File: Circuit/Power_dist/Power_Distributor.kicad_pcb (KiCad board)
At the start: 2 copper layers, 150.2 x 108.9 mm, 97 parts, among them CON1 Conn-PCIE-x16, J1 Thruster_Off_Switch, P1 XT60, P11 XT60, P15 USB_B, P16 XT60, P17 XT60, P2 XT30, P3 XT30, P4 XT30, P5 XT30, Q1 IPD90P03P4L, Q2 IPD90P03P4L, Q3 IPD90P03P4L, Q5 IPD90P03P4L, Q6 AUIRFS8409-7P, Q7 AUIRFS8409-7P, U1 93LC56BT-I/OT, U2 FT232H, U3 ACPL-247-500E, U4 ACPL-247-500E, U5 LTC4357, U6 LTC4357, U7 UWE-12/6-Q12P, U8 TEN_20-2411WIN, Y1 12MHz

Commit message: route pcb except gnd
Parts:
- moved C13 42.4 mm to (100.3, 116.6)
- moved C14 42.4 mm to (94.2, 113.5)
- moved C15 42.4 mm to (100.0, 113.5)
- moved C17 42.4 mm to (106.1, 113.5)
- moved C3 42.4 mm to (58.4, 107.4)
- moved C5 42.4 mm to (89.0, 121.2)
- moved C6 42.4 mm to (81.5, 112.0)
- moved C7 42.4 mm to (94.2, 110.5)
- moved C8 42.4 mm to (83.6, 121.2)
- moved D7 42.4 mm to (74.9, 117.3)
- moved L2 42.4 mm to (100.1, 110.5)
- moved P15 42.4 mm to (58.7, 126.7)
- moved R10 42.4 mm to (70.2, 117.3)
- moved R17 42.4 mm to (73.6, 106.4)
- moved R18 42.4 mm to (64.7, 117.3)
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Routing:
- net +BATT: track 0.00 -> 356.9 mm
- net +5V: track 0.00 -> 218.3 mm, vias 0 -> 2
- net /Kill_SW: track 5.00 -> 174.6 mm, vias 0 -> 1
- net +12V: track 0.00 -> 165.6 mm
- net /Power_Controller/SW1_C: track 14.3 -> 175.4 mm, vias 0 -> 2
- net /Power_Controller/SW4_C: track 15.8 -> 138.2 mm, vias 0 -> 2
- net /Power_Controller/SW3_C: track 30.8 -> 152.7 mm, vias 0 -> 2
- net Net-(C12-Pad1): track 9.53 -> 119.1 mm, vias 0 -> 2
- net +3V3: track 108.7 -> 175.0 mm, vias 0 -> 2
- net /Power_Controller/SW2_C: track 18.1 -> 73.5 mm, vias 0 -> 2
- net Net-(JP1-Pad2): track 0.00 -> 53.3 mm
- net Net-(D8-Pad2): track 0.00 -> 36.9 mm
- net Net-(D13-Pad2): track 0.00 -> 33.9 mm
- net Net-(F2-Pad2): track 0.00 -> 31.5 mm
- net Net-(C13-Pad1): track 37.3 -> 63.2 mm
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
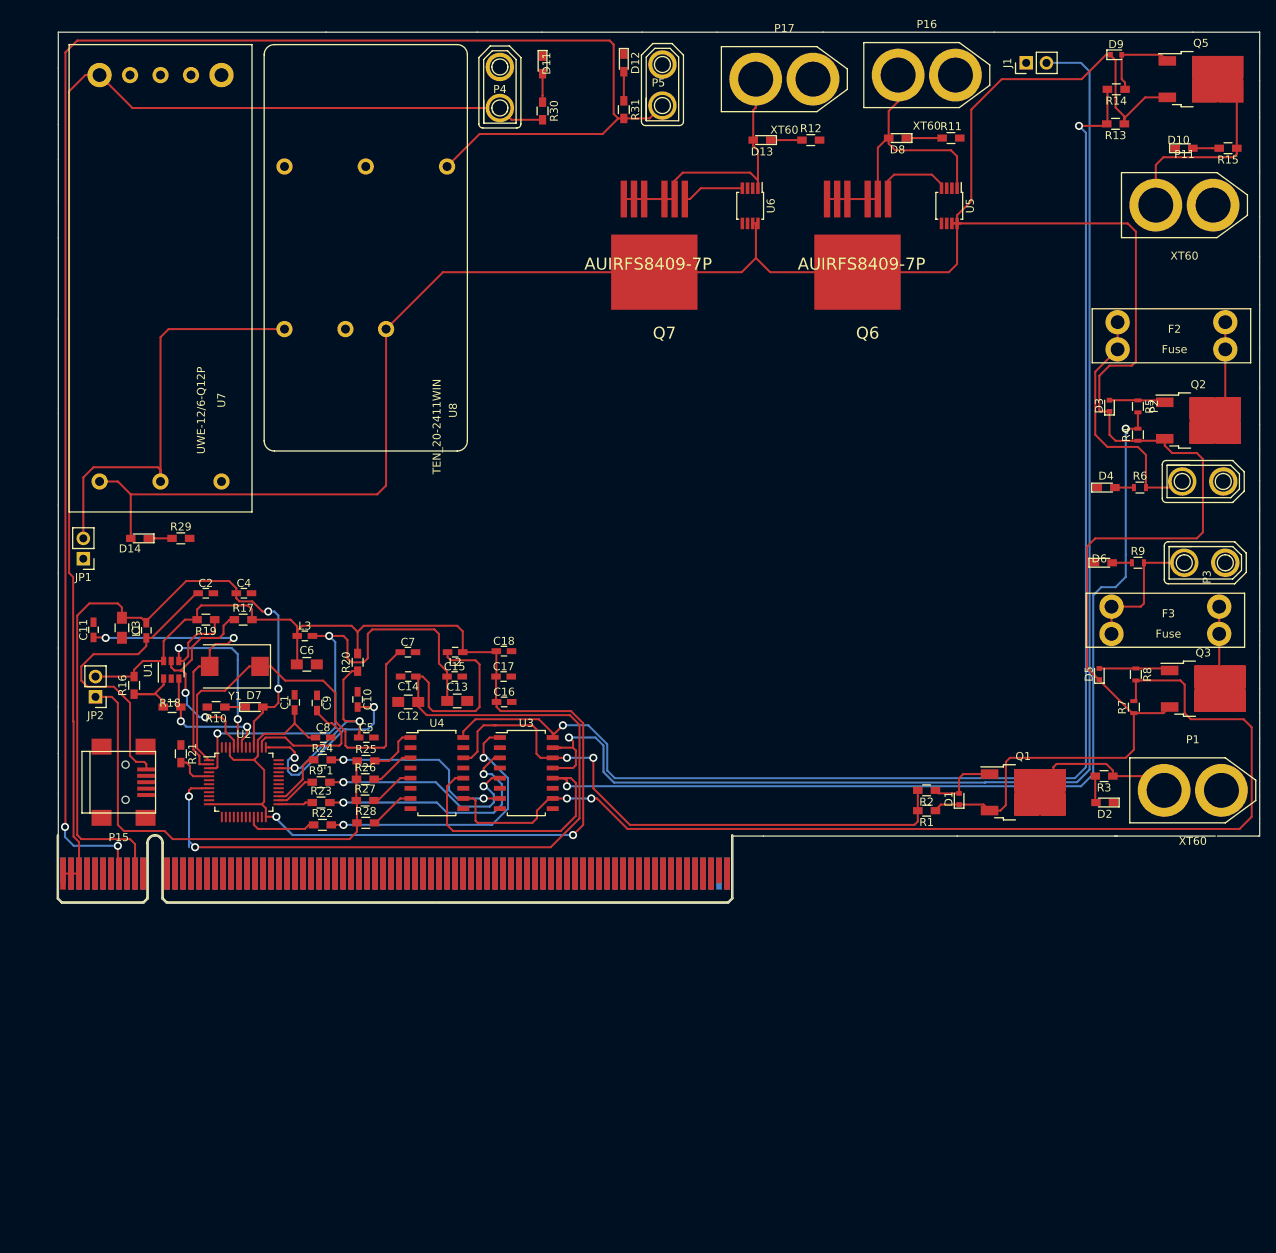
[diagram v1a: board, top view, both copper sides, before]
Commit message: add Vbatt plane, re-arrange components
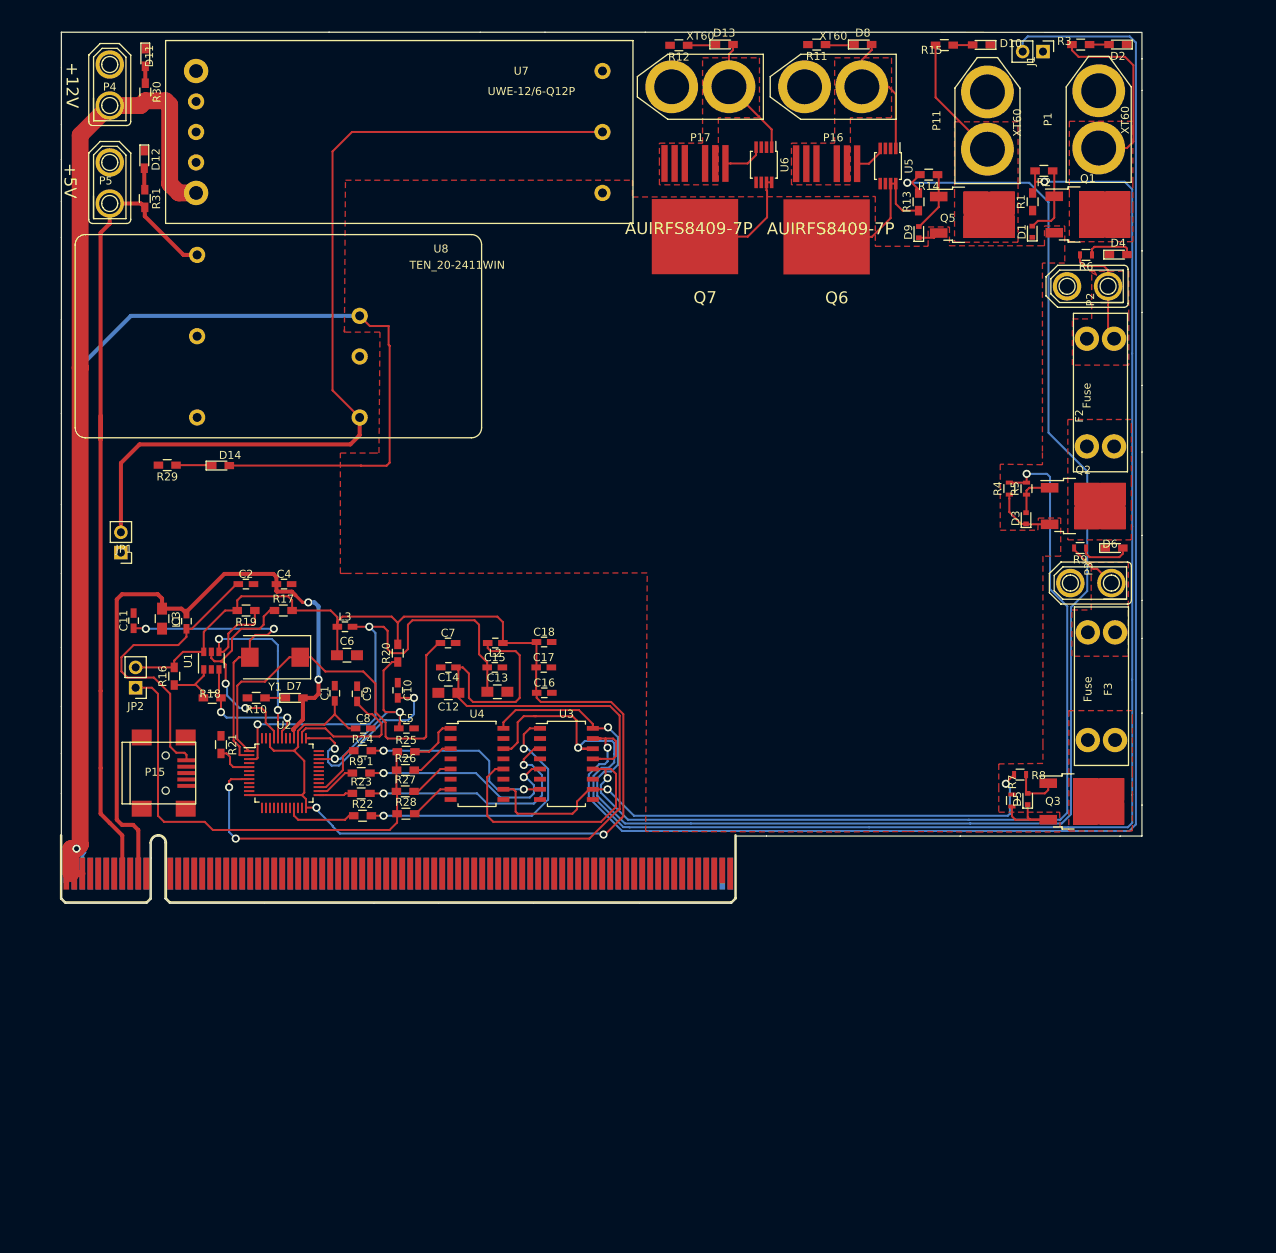
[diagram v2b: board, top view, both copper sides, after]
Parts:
- moved D2 94.8 mm to (182.9, 34.5)
- moved R3 91.5 mm to (178.3, 34.5), turned to 0 degrees
- moved P1 84.7 mm to (180.5, 43.9), turned to 90 degrees
- moved R2 78.8 mm to (173.7, 50.3)
- moved R1 77.3 mm to (172.3, 54.2), turned to 90 degrees
- moved Q1 72.7 mm to (179.2, 55.8)
- moved U7 72.5 mm to (118.5, 53.1), turned to 180 degrees
- moved D1 71.5 mm to (172.2, 57.9)
- moved P5 70.2 mm to (56.9, 52.1)
- moved D12 61.1 mm to (61.2, 48.9)
- moved R31 60.9 mm to (61.3, 53.8)
- moved R30 49.7 mm to (61.3, 40.5)
- moved D11 49.7 mm to (61.3, 36.2)
- moved P4 48.8 mm to (56.9, 39.8)
- moved R15 37.7 mm to (161.2, 34.6), turned to 0 degrees
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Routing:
- net +BATT: track 356.9 -> 197.8 mm
- net /Power_Controller/SW2_C: track 73.5 -> 197.0 mm
- net +5V: track 218.3 -> 102.6 mm, vias 2 -> 0
- net /Power_Controller/SW4_C: track 138.2 -> 75.5 mm
- net Net-(JP1-Pad2): track 53.3 -> 111.6 mm
- net +12V: track 165.6 -> 127.3 mm, vias 0 -> 1
- net /Kill_SW: track 174.6 -> 203.0 mm
- net Net-(D8-Pad2): track 36.9 -> 17.2 mm
- net Net-(D13-Pad2): track 33.9 -> 15.3 mm
- net Net-(F2-Pad2): track 31.5 -> 13.8 mm
- net /Power_Controller/SW1_C: track 175.4 -> 189.9 mm
- net Net-(F3-Pad2): track 17.8 -> 6.59 mm
- net Net-(F2-Pad1): track 10.9 -> 0.00 mm
- net Net-(F3-Pad1): track 10.3 -> 0.00 mm
- net Net-(P11-Pad1): track 23.8 -> 15.7 mm
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- added copper zone on F.Cu, net +BATT
- added copper zone on F.Cu, net Net-(D13-Pad2)
- added copper zone on F.Cu, net Net-(D8-Pad2)
- added copper zone on F.Cu, net Net-(F2-Pad1)
- added copper zone on F.Cu, net Net-(F2-Pad2)
- added copper zone on F.Cu, net Net-(F3-Pad1)
- added copper zone on F.Cu, net Net-(F3-Pad2)
- added copper zone on F.Cu, net Net-(P1-Pad1)
- added copper zone on F.Cu, net Net-(P11-Pad1)
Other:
- board size 150.2 x 108.9 mm -> 135.1 x 108.9 mm
- board text added: "+12V"
- board text added: "+5V"

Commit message: gnd planes finish routing
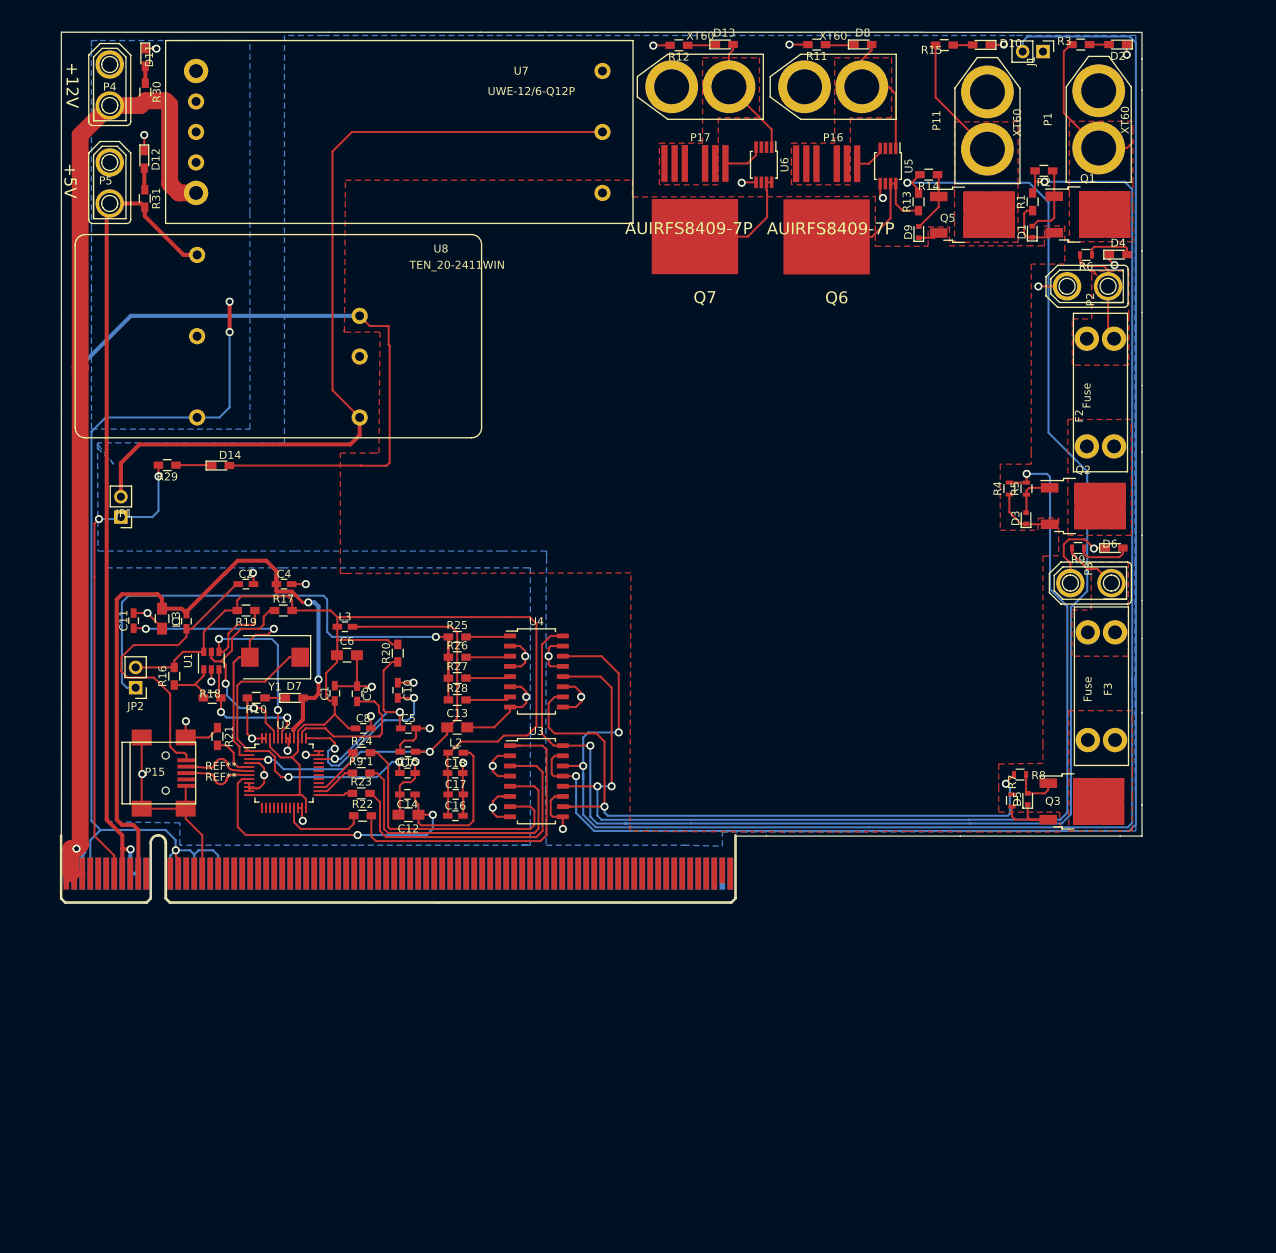
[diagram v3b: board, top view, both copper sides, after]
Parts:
- added REF**: 0, mw_inductor, F.Cu at (67.8, 124.8)
- added REF**: 0, mw_inductor, F.Cu at (73.8, 125.9)
- moved C18 19.8 mm to (100.1, 125.6)
- moved C17 19.3 mm to (100.1, 128.3)
- moved C16 19.0 mm to (100.1, 130.9)
- moved C7 17.0 mm to (94.1, 125.6)
- moved C14 16.7 mm to (94.1, 128.3)
- moved C12 16.0 mm to (94.2, 130.8)
- moved R25 15.7 mm to (100.3, 108.6)
- moved R28 15.6 mm to (100.3, 116.5)
- moved R27 15.6 mm to (100.3, 113.7)
- moved R26 15.5 mm to (100.3, 111.1)
- moved C15 15.1 mm to (94.2, 122.9), turned to 180 degrees
- moved L2 14.6 mm to (100.1, 123.1), turned to 0 degrees
- moved U4 13.7 mm to (110.2, 112.9)
- moved C13 6.70 mm to (100.3, 119.9)
- moved JP1 4.44 mm to (58.3, 93.6)
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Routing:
- net GNDD: track 0.00 -> 131.6 mm, vias 0 -> 21
- net GNDREF: track 0.00 -> 119.5 mm, vias 0 -> 5
- net GND: track 0.00 -> 105.5 mm, vias 0 -> 14
- net Net-(C12-Pad1): track 118.3 -> 56.3 mm
- net +3V3: track 175.9 -> 145.1 mm, vias 2 -> 0
- net Net-(JP2-Pad1): track 58.3 -> 71.0 mm, vias 0 -> 1
- net Net-(C7-Pad1): track 53.9 -> 41.6 mm, vias 0 -> 2
- net Net-(R24-Pad2): track 24.6 -> 34.3 mm, vias 2 -> 0
- net /Power_Controller/SW4_C: track 75.5 -> 85.0 mm
- net Net-(R9'1-Pad2): track 27.1 -> 36.5 mm, vias 2 -> 0
- net /Power_Controller/SW3_C: track 146.6 -> 137.3 mm, vias 2 -> 3
- net +BATT: track 197.8 -> 205.8 mm
- net Net-(C13-Pad1): track 63.2 -> 55.6 mm
- net Net-(R23-Pad2): track 31.1 -> 38.0 mm, vias 2 -> 0
- net /Kill_SW: track 203.0 -> 196.2 mm
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- added copper zone on B.Cu, net GND
- added copper zone on B.Cu, net GNDD
- added copper zone on B.Cu, net GNDREF

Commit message: finish zeabus 2018 Powerdistributor Board Ver 1
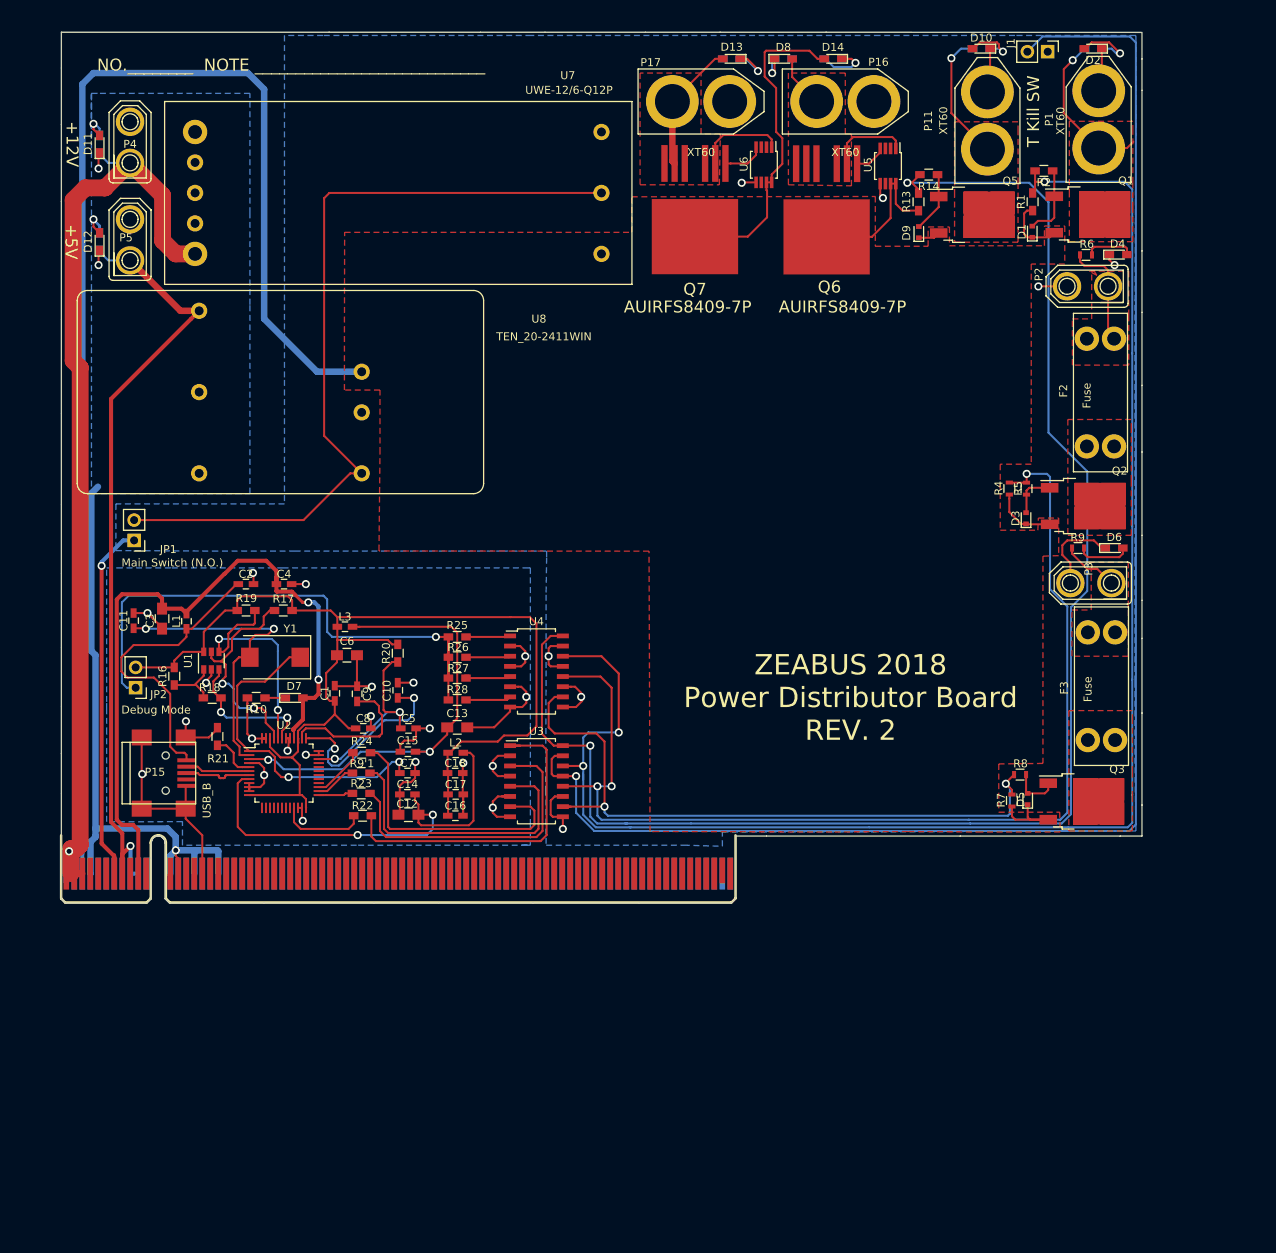
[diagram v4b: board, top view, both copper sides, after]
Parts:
- removed REF** (x2): 0, mw_inductor
- JP2: value Jumper -> Debug Mode
- R11, R12, R15, R29, R3, R30, R31: moved to B.Cu
- moved R29 97.5 mm to (147.3, 36.3), turned to 0 degrees
- moved D14 91.9 mm to (147.3, 36.3), turned to 180 degrees
- moved D11 12.3 mm to (55.6, 47.0), turned to 90 degrees
- moved D12 11.7 mm to (55.6, 59.2), turned to 90 degrees
- moved D8 10.1 mm to (141.1, 36.3)
- moved R30 8.67 mm to (55.6, 47.0)
- moved R31 7.81 mm to (55.6, 59.2)
- moved U7 7.62 mm to (118.4, 60.7)
- moved P4 7.60 mm to (59.4, 47.0)
- moved P5 7.55 mm to (59.4, 59.2)
- moved U8 6.99 mm to (88.4, 75.4)
- moved R12 6.80 mm to (134.6, 36.3)
- moved R15 4.63 mm to (165.8, 35.1)
- moved R11 4.53 mm to (141.1, 36.3), turned to 0 degrees
- moved JP1 3.36 mm to (59.9, 96.5)
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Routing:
- net +BATT: track 205.8 -> 257.5 mm
- net Net-(D13-Pad2): track 15.3 -> 27.6 mm
- net GNDREF: track 119.5 -> 107.5 mm, vias 5 -> 3
- net /Power_Controller/D+: track 1.33 -> 8.38 mm
- net GND: track 105.5 -> 98.6 mm, vias 14 -> 8
- net /Power_Controller/D-: track 2.20 -> 8.97 mm
- net Net-(D2-Pad2): track 2.44 -> 7.84 mm, vias 0 -> 1
- net Net-(JP1-Pad2): track 107.1 -> 102.2 mm
- net Net-(D10-Pad2): track 2.45 -> 6.60 mm, vias 0 -> 1
- net +12V: track 127.3 -> 124.2 mm
- net Net-(D12-Pad2): track 2.72 -> 5.70 mm, vias 0 -> 1
- net +5V: track 104.1 -> 101.5 mm
- net Net-(D13-Pad1): track 3.51 -> 5.77 mm, vias 0 -> 1
- net Net-(D14-Pad1): track 4.48 -> 6.58 mm, vias 0 -> 1
- net /Power_Controller/SW4_C: track 85.0 -> 86.7 mm
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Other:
- outline, holes or cut-outs redrawn
- board text added: "NO.________ NOTE ____________________________"
- board text added: "T Kill SW"
- board text added: "ZEABUS 2018 Power Distributor Board REV. 2"
